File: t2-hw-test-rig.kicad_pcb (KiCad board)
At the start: 2 copper layers, 86.4 x 94 mm, 153 parts, among them J101 CONN_01X02, J102 BARREL_JACK, J103 CONN_01X02, J201 MICROUSB-TH, J202 CONN_01X02, J203 MICROUSB-TH, J204 USB_A_TH, J301 CONN_02x05, 0.05", Q101 pMOS, Q401 CJ2302, Q402 CJ2302, Q403 CJ2302, Q404 CJ2302, Q405 CJ2302 DNP, Q406 CJ2302 DNP, SW301 Switch_DPST, SW302 Switch_DPST, U101 MAX6102, U102 XC6206P332MR-G, U301 ATSAMD21J18A-MUT, U302 AAT4610, U303 AAT4610, U401 MAX9919FASA+, U402 MAX9919FASA+, U403 MAX9919FASA+, U404 MAX9919FASA+, U405 MAX9919FASA+, U501 TSV324IDT, U502 TSV324IDT, U503 TSV324IDT, X301 FC-135

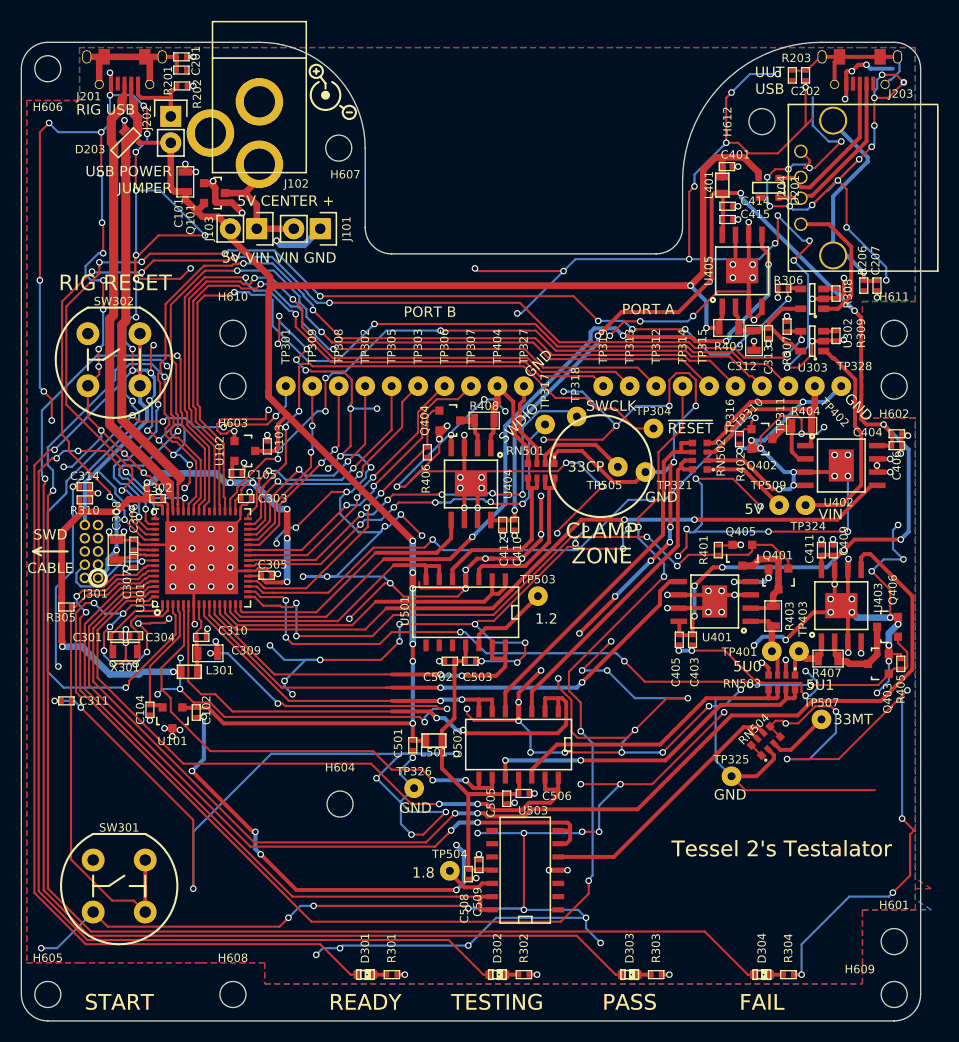
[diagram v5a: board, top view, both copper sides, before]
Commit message: soic-8-1ep footprint fix, moved mount holes for mech clearance
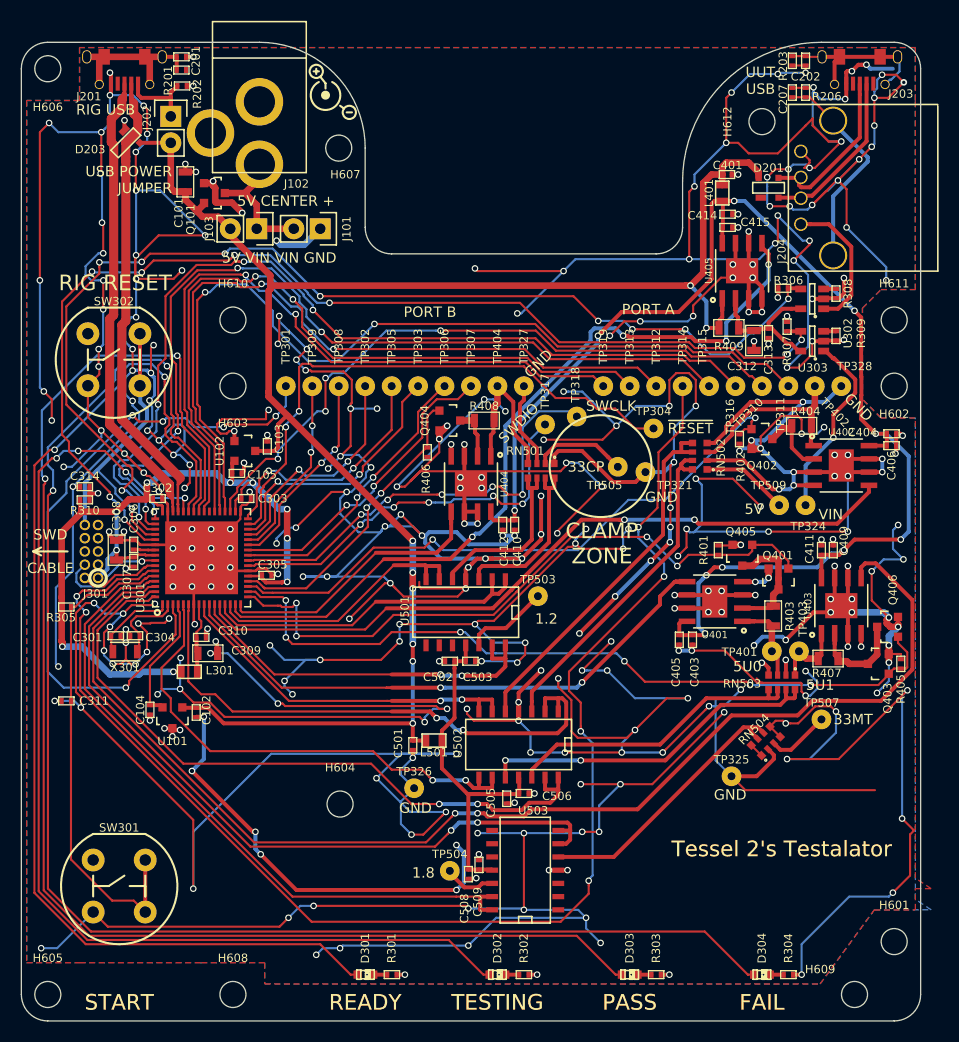
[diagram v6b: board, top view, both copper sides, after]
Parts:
- moved C207 20.2 mm to (124.8, 63.2), turned to 90 degrees
- moved R206 19.4 mm to (126.1, 63.2), turned to 90 degrees
- moved H609 3.81 mm to (130.8, 149.9)
- moved C202 1.40 mm to (126.1, 60.2)
- moved R203 1.40 mm to (124.8, 60.2)
- moved H610 1.27 mm to (71.1, 85.1)
- moved H611 1.27 mm to (134.6, 85.1)
- moved C401 0.76 mm to (118.6, 71.1)
- moved C414 0.76 mm to (118.6, 74.9)
- moved C415 0.76 mm to (118.6, 76.2)
- moved L401 0.76 mm to (118.1, 72.9)
- moved C404 0.51 mm to (134.4, 96.0)
- moved C406 0.51 mm to (134.4, 97.2)
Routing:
- net GND: track 1588.3 -> 1628.0 mm, vias 347 -> 348
- net /SAM/UUT_VIN: track 20.7 -> 18.2 mm, vias 0 -> 1
- net +5V: track 180.5 -> 178.2 mm
- net UUT_5VUSB0: track 7.35 -> 8.50 mm
- net UUT_5V_UPSTREAM: track 13.4 -> 14.5 mm
- net I_PB33: track 25.6 -> 26.7 mm
- net /CURRENT/5VUSB1_RS-: track 8.77 -> 9.80 mm
- net /CURRENT/5VUSB0_RS-: track 10.6 -> 11.6 mm
- net /USB/UUT_USB_SHELL: track 22.4 -> 21.6 mm, vias 1 -> 0
- net I_USB0: track 54.4 -> 55.2 mm
- net UUT_5VUSB1: track 6.33 -> 7.13 mm
- net UUT_33PB: track 14.8 -> 15.6 mm
- net /CURRENT/33PB_RS-: track 4.13 -> 4.93 mm
- net I_USB1: track 119.7 -> 118.9 mm
- net /SAM/PORT_A_MISO: track 84.4 -> 85.1 mm
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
